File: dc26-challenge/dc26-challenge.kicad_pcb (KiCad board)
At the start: 2 copper layers, 107 x 107 mm, 0 parts

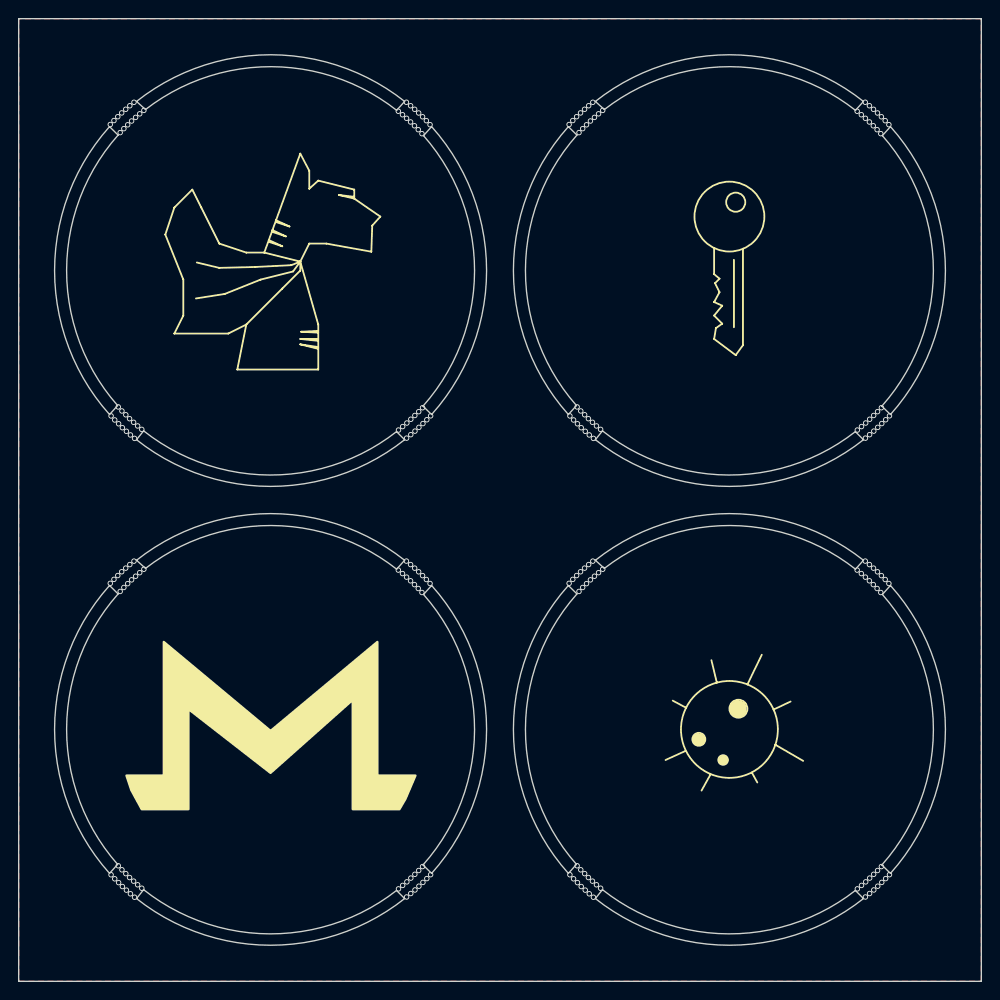
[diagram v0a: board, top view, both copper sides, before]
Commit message: Challenge coin icons almost complete
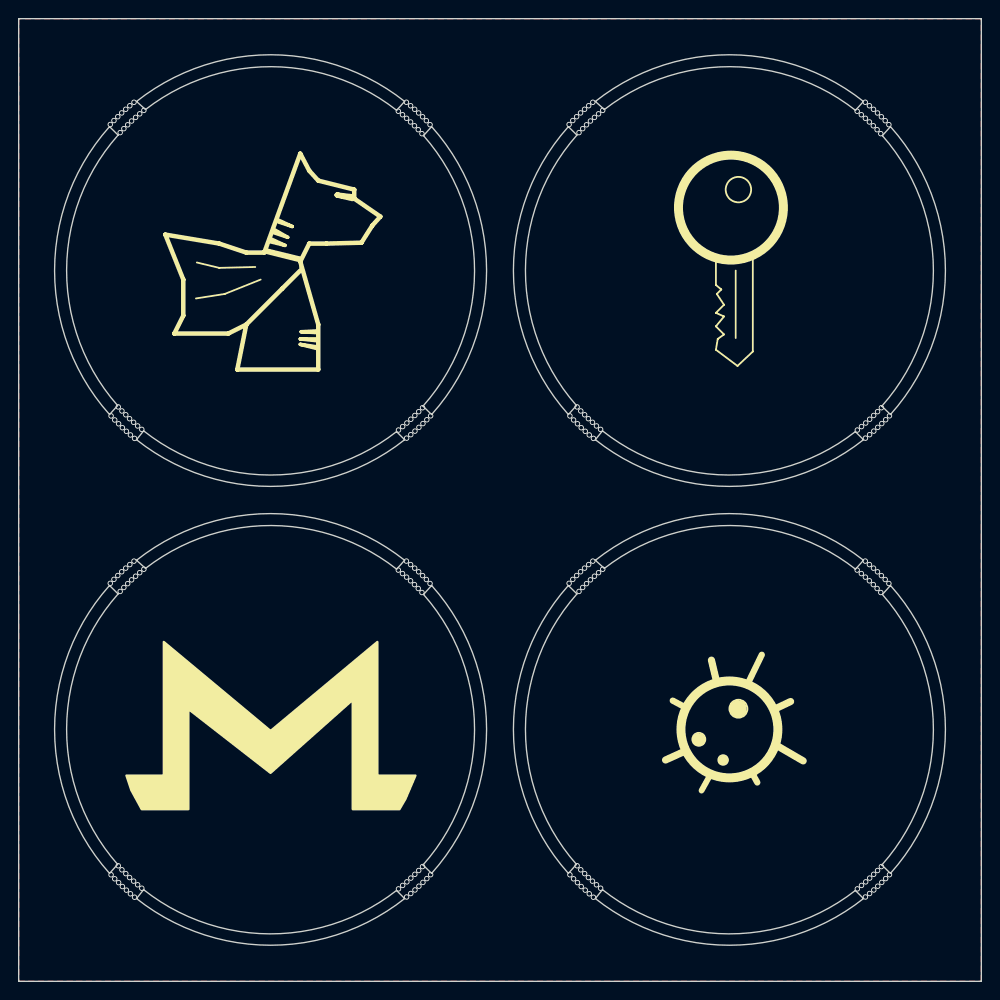
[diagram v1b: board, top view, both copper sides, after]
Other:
- board text added: "3b, 17, 15, 13, 13, 0d, 0c, 5a, 21, 1b, 11, 03, 52, 1d, 04, 02, 44, 14, 42, 50, 1f, 06, 4e, 05, 09, 47, 50, 0c, 02, 43, 13, 0a, 45, 5a, 02, 01, 11, 13, 4c, 11, 17, 4c, 00, 08, 0f, 49, 19, 5e, 4e, 02, 07, 52, 04, 0a, 03, 0d, 4b, 42, 41, 14, 16, 4e, 0c, 09, 56, 19, 00, 4c, 10, 02, 10, 49, 1f, 01"
- board text added: "@mymonero @fluffypony @elasticninja"

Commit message: Final icons + ciphertext
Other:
- board text added: "33, 17, 15, 13, 13, 0d, 47, 08, 13, 1e, 09, 1f, 0c, 50, 11, 04, 06, 47, 12, 52, 1b, 11, 1a, 08, 05, 45, 50, 04, 02, 07, 47, 11, 54, 0f, 16, 17, 41, 09, 46, 50, 0d, 05, 07, 0e, 0c, 47, 5a, 1b, 00, 07, 09, 52, 1d, 04, 18, 0a, 8, 0c"
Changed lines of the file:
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@@
     (effects (font (size 1.5 1.5) (thickness 0.25)) (justify mirror))
   )
-  (gr_text "3b, 17, 15, 13, 13, 0d, 0c, 5a, \n21, 1b, 11, 03, 52, 1d, 04, 02, \n44, 14, 42, 50, 1f, 06, 4e, 05, \n09, 47, 50, 0c, 02, 43, 13, 0a, \n45, 5a, 02, 01, 11, 13, 4c, 11, \n17, 4c, 00, 08, 0f, 49, 19, 5e, \n4e, 02, 07, 52, 04, 0a, 03, 0d, \n4b, 42, 41, 14, 16, 4e, 0c, 09, \n56, 19, 00, 4c, 10, 02, 10, 49, \n1f, 01" (at 125.7 69.9) (layer B.SilkS)
+  (gr_text "33, 17, 15, 13, 13, 0d, 47, 08, \n13, 1e, 09, 1f, 0c, 50, 11, 04, \n06, 47, 12, 52, 1b, 11, 1a, 08, \n05, 45, 50, 04, 02, 07, 47, 11, \n54, 0f, 16, 17, 41, 09, 46, 50, \n0d, 05, 07, 0e, 0c, 47, 5a, 1b, \n00, 07, 09, 52, 1d, 04, 18, 0a, \n8, 0c" (at 125.7 69.9) (layer B.SilkS)
     (effects (font (size 1.5 1.5) (thickness 0.25)) (justify mirror))
   )

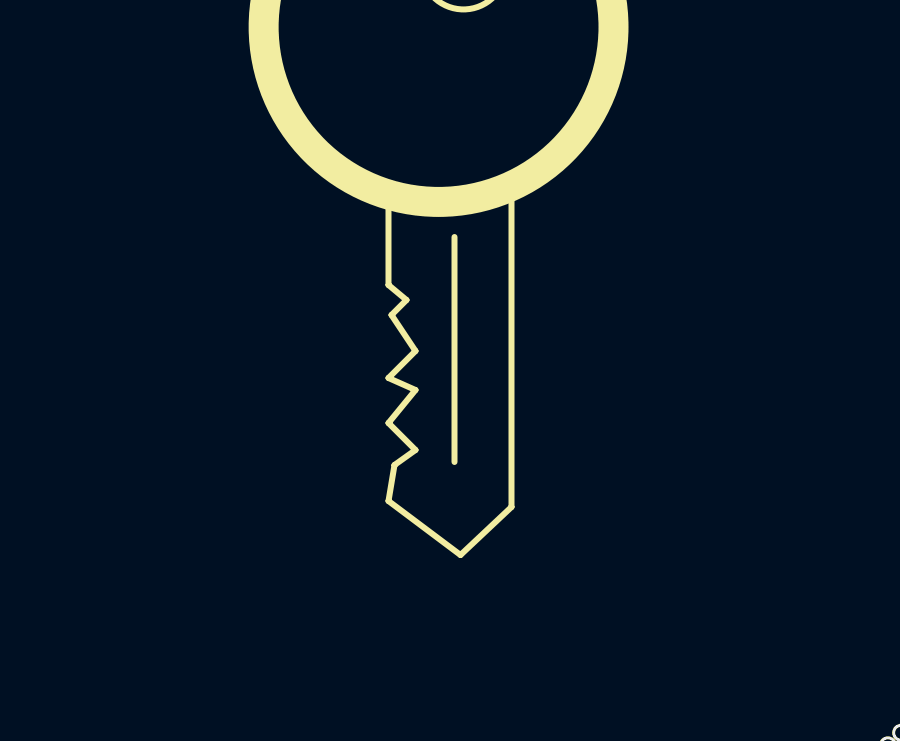
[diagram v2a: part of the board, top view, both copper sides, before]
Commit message: More fixes for challenge coins
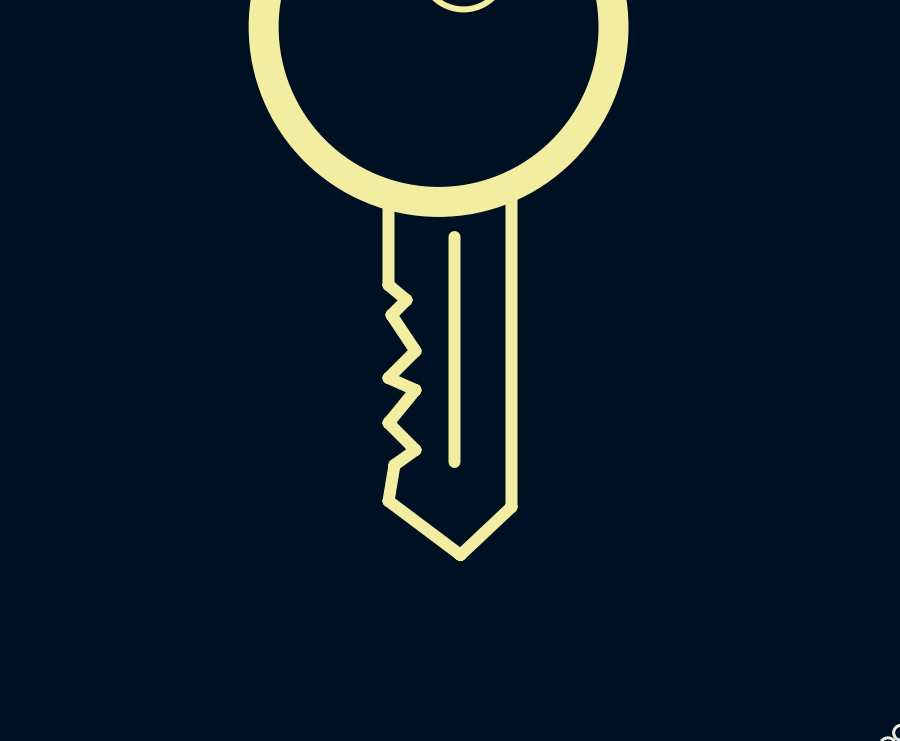
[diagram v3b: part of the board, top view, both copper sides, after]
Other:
- board text added: "33, 17, 15, 13, 13, 0d, 43, 0f, 00, 1c, 04, 08, 43, 09, 49, 4c, 07, 0e, 05, 49, 0e, 13, 02, 41, 05, 55, 02, 17, 09, 0d, 04, 1b, 00, 0e, 1a, 0f, 15, 46, 55, 03, 00, 1f, 43, 04, 10, 59, 0a, 06, 01, 06, 14, 41, 00, 0d, 15, 43, 13, 0d, 00, 09, 17, 0d, 14, 14, 45, 50, 11, 1e, 02, 09, 11, 41, 19, 06, 07, 0e, 08, 53"
- board text added: "33, 17, 15, 13, 13, 0d, 53, 0a, 1d, 1c, 08, 02, 49, 05, 08, 40, 43, 06, 42, 50, 08, 1d, 1a, 0e, 1c, 4f, 11, 0b, 4c, 17, 0f, 03, 54, 5a, 11, 0f, 0f, 46, 43, 11, 10, 1f, 06, 47, 05, 41, 09, 06, 1c, 0e, 4b, 49, 1e, 11, 09, 10, 13, 0b, 4e, 1b, 1e, 4e, 08, 0a, 4c, 1e, 00, 1f, 10, 47, 15, 49, 0e, 1a, 4e, 05, 0f, 41, 02, 17, 04, 06, 06, 42, 49, 14, 52, 06, 14, 0b, 41, 1e, 16"
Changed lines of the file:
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@@
     (uvia_drill 0.1)
   )
-  (gr_text "3b, 17, 15, 13, 13, 0d, 0c, 5a, \n21, 1b, 11, 03, 52, 1d, 04, 02, \n44, 14, 42, 50, 1f, 06, 4e, 05, \n09, 47, 50, 0c, 02, 43, 13, 0a, \n45, 5a, 02, 01, 11, 13, 4c, 11, \n17, 4c, 00, 08, 0f, 49, 19, 5e, \n4e, 02, 07, 52, 04, 0a, 03, 0d, \n4b, 42, 41, 14, 16, 4e, 0c, 09, \n56, 19, 00, 4c, 10, 02, 10, 49, \n1f, 01" (at 125.5 121.2) (layer B.SilkS)
-    (effects (font (size 1.5 1.5) (thickness 0.25)) (justify mirror))
+  (gr_text "33, 17, 15, 13, 13, 0d, 53, 0a, \n1d, 1c, 08, 02, 49, 05, 08, 40, \n43, 06, 42, 50, 08, 1d, 1a, 0e, \n1c, 4f, 11, 0b, 4c, 17, 0f, 03, \n54, 5a, 11, 0f, 0f, 46, 43, 11, \n10, 1f, 06, 47, 05, 41, 09, 06, \n1c, 0e, 4b, 49, 1e, 11, 09, 10, \n13, 0b, 4e, 1b, 1e, 4e, 08, 0a, \n4c, 1e, 00, 1f, 10, 47, 15, 49, \n0e, 1a, 4e, 05, 0f, 41, 02, 17, \n04, 06, 06, 42, 49, 14, 52, 06, \n14, 0b, 41, 1e, 16" (at 125 120.6) (layer B.SilkS)
+    (effects (font (size 1.3 1.5) (thickness 0.25)) (justify mirror))
   )
-  (gr_text "3b, 17, 15, 13, 13, 0d, 0c, 5a, \n21, 1b, 11, 03, 52, 1d, 04, 02, \n44, 14, 42, 50, 1f, 06, 4e, 05, \n09, 47, 50, 0c, 02, 43, 13, 0a, \n45, 5a, 02, 01, 11, 13, 4c, 11, \n17, 4c, 00, 08, 0f, 49, 19, 5e, \n4e, 02, 07, 52, 04, 0a, 03, 0d, \n4b, 42, 41, 14, 16, 4e, 0c, 09, \n56, 19, 00, 4c, 10, 02, 10, 49, \n1f, 01" (at 74.2 121.3) (layer B.SilkS)
+  (gr_text "33, 17, 15, 13, 13, 0d, 43, 0f, \n00, 1c, 04, 08, 43, 09, 49, 4c, \n07, 0e, 05, 49, 0e, 13, 02, 41, \n05, 55, 02, 17, 09, 0d, 04, 1b, \n00, 0e, 1a, 0f, 15, 46, 55, 03, \n00, 1f, 43, 04, 10, 59, 0a, 06, \n01, 06, 14, 41, 00, 0d, 15, 43, \n13, 0d, 00, 09, 17, 0d, 14, 14, \n45, 50, 11, 1e, 02, 09, 11, 41, \n19, 06, 07, 0e, 08, 53" (at 74.2 120.4) (layer B.SilkS)
     (effects (font (size 1.5 1.5) (thickness 0.25)) (justify mirror))
   )
@@
     (effects (font (size 1.5 1.5) (thickness 0.25)) (justify mirror))
   )
-  (gr_line (start 124.7 77.6) (end 124.5 78.8) (layer F.SilkS) (width 0.2))
-  (gr_line (start 125.4 77.1) (end 124.7 77.6) (layer F.SilkS) (width 0.2))
-  (gr_line (start 124.5 76.2) (end 125.4 77.1) (layer F.SilkS) (width 0.2))
-  (gr_line (start 125.4 75.1) (end 124.5 76.2) (layer F.SilkS) (width 0.2))
-  (gr_line (start 124.5 74.7) (end 125.4 75.1) (layer F.SilkS) (width 0.2))
+  (gr_line (start 124.7 77.6) (end 124.5 78.8) (layer F.SilkS) (width 0.4))
+  (gr_line (start 125.4 77.1) (end 124.7 77.6) (layer F.SilkS) (width 0.4))
+  (gr_line (start 124.5 76.2) (end 125.4 77.1) (layer F.SilkS) (width 0.4))
+  (gr_line (start 125.4 75.1) (end 124.5 76.2) (layer F.SilkS) (width 0.4))
+  (gr_line (start 124.5 74.7) (end 125.4 75.1) (layer F.SilkS) (width 0.4))
   (gr_circle (center 125.3 124.4) (end 125.8 124.6) (layer F.SilkS) (width 0.2))
   (gr_circle (center 122.6 122.1) (end 123.2 122.5) (layer F.SilkS) (width 0.2))
@@
   (gr_line (start 128 116) (end 129.6 112.7) (layer F.SilkS) (width 0.7))
   (gr_circle (center 126 121) (end 131 119) (layer F.SilkS) (width 1))
-  (gr_line (start 126.7 70) (end 126.7 77.5) (layer F.SilkS) (width 0.2))
-  (gr_line (start 128.6 79) (end 128.6 68.3) (layer F.SilkS) (width 0.2))
-  (gr_line (start 126.9 80.6) (end 128.6 79) (layer F.SilkS) (width 0.2))
-  (gr_line (start 124.5 78.8) (end 126.9 80.6) (layer F.SilkS) (width 0.2))
-  (gr_line (start 125.4 73.8) (end 124.5 74.7) (layer F.SilkS) (width 0.2))
-  (gr_line (start 124.6 72.6) (end 125.4 73.8) (layer F.SilkS) (width 0.2))
-  (gr_line (start 125.1 72.1) (end 124.6 72.6) (layer F.SilkS) (width 0.2))
-  (gr_line (start 124.5 71.6) (end 125.1 72.1) (layer F.SilkS) (width 0.2))
-  (gr_line (start 124.5 68.7) (end 124.5 71.6) (layer F.SilkS) (width 0.2))
+  (gr_line (start 126.7 70) (end 126.7 77.5) (layer F.SilkS) (width 0.4))
+  (gr_line (start 128.6 79) (end 128.6 68.3) (layer F.SilkS) (width 0.4))
+  (gr_line (start 126.9 80.6) (end 128.6 79) (layer F.SilkS) (width 0.4))
+  (gr_line (start 124.5 78.8) (end 126.9 80.6) (layer F.SilkS) (width 0.4))
+  (gr_line (start 125.4 73.8) (end 124.5 74.7) (layer F.SilkS) (width 0.4))
+  (gr_line (start 124.6 72.6) (end 125.4 73.8) (layer F.SilkS) (width 0.4))
+  (gr_line (start 125.1 72.1) (end 124.6 72.6) (layer F.SilkS) (width 0.4))
+  (gr_line (start 124.5 71.6) (end 125.1 72.1) (layer F.SilkS) (width 0.4))
+  (gr_line (start 124.5 68.7) (end 124.5 71.6) (layer F.SilkS) (width 0.4))
   (gr_circle (center 127 61) (end 128 62) (layer F.SilkS) (width 0.2))
   (gr_circle (center 126.169049 63) (end 131.169049 66) (layer F.SilkS) (width 1))
